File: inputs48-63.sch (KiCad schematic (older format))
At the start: 160 parts

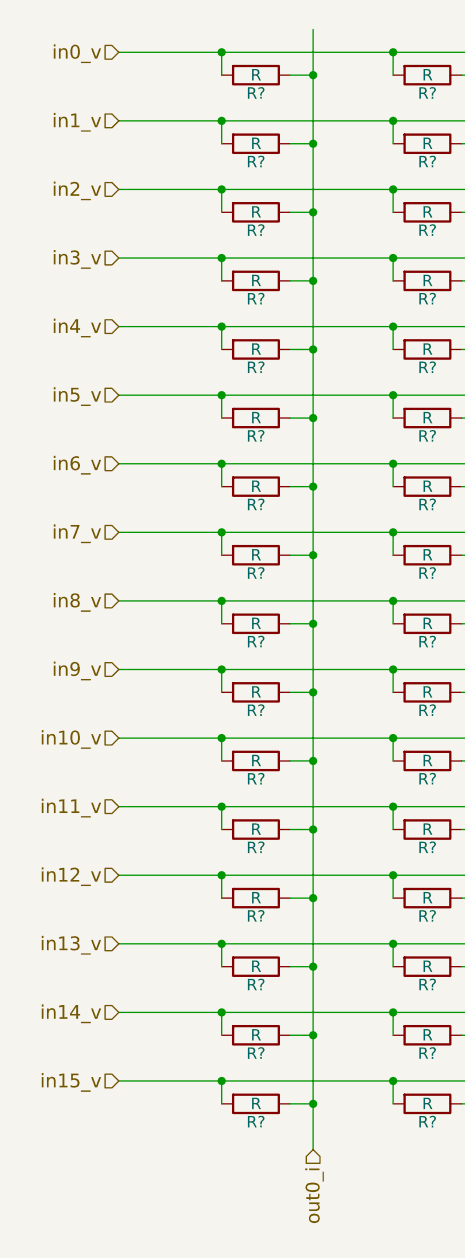
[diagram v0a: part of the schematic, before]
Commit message: updated labels for schematics 32-47 and 48-63
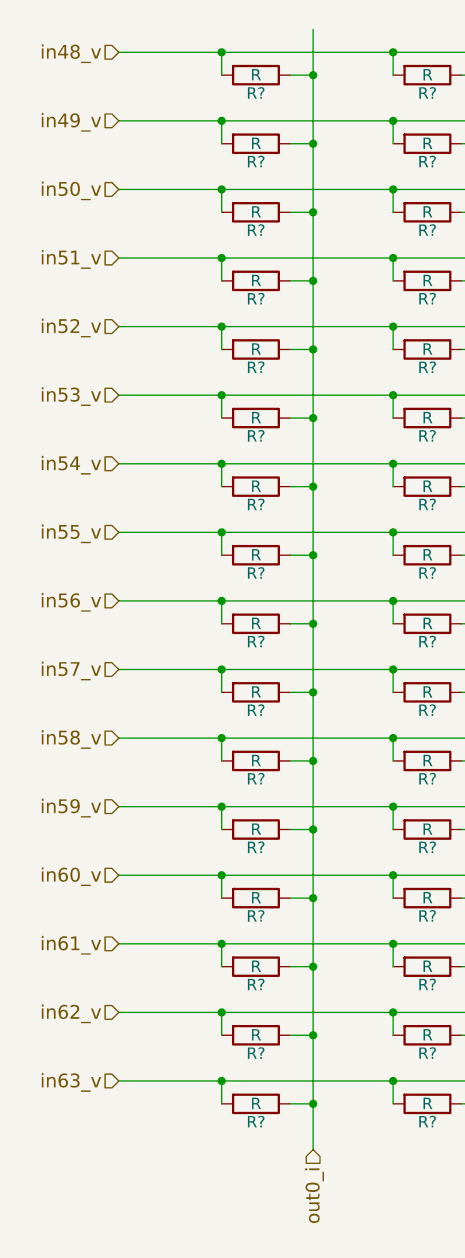
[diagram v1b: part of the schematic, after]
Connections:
- net labels added: in48_v, in49_v, in50_v, in51_v, in52_v, in53_v, in54_v, in55_v, in56_v, in57_v, in58_v, in59_v, in60_v, in61_v, in62_v, in63_v
- net labels removed: in0_v, in10_v, in11_v, in12_v, in13_v, in14_v, in15_v, in1_v, in2_v, in3_v, in4_v, in5_v, in6_v, in7_v, in8_v, in9_v
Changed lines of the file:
@@
 $EndDescr
 Text HLabel 1900 1050 0    60   Input ~ 0
-in0_v
+in48_v
 Text HLabel 1900 1350 0    60   Input ~ 0
-in1_v
+in49_v
 Text HLabel 1900 1650 0    60   Input ~ 0
-in2_v
+in50_v
 Text HLabel 1900 1950 0    60   Input ~ 0
-in3_v
+in51_v
 Text HLabel 1900 2250 0    60   Input ~ 0
-in4_v
+in52_v
 Text HLabel 1900 2550 0    60   Input ~ 0
-in5_v
+in53_v
 Text HLabel 1900 2850 0    60   Input ~ 0
-in6_v
+in54_v
 Text HLabel 1900 3150 0    60   Input ~ 0
-in7_v
+in55_v
 Text HLabel 1900 3450 0    60   Input ~ 0
-in8_v
+in56_v
 Text HLabel 1900 3750 0    60   Input ~ 0
-in9_v
+in57_v
 Text HLabel 1900 4050 0    60   Input ~ 0
-in10_v
+in58_v
 Text HLabel 1900 4350 0    60   Input ~ 0
-in11_v
+in59_v
 Text HLabel 1900 4650 0    60   Input ~ 0
-in12_v
+in60_v
 Text HLabel 1900 4950 0    60   Input ~ 0
-in13_v
+in61_v
 Text HLabel 1900 5250 0    60   Input ~ 0
-in14_v
+in62_v
 Text HLabel 1900 5550 0    60   Input ~ 0
-in15_v
+in63_v
 Text HLabel 2750 5850 3    60   Input ~ 0
 out0_i

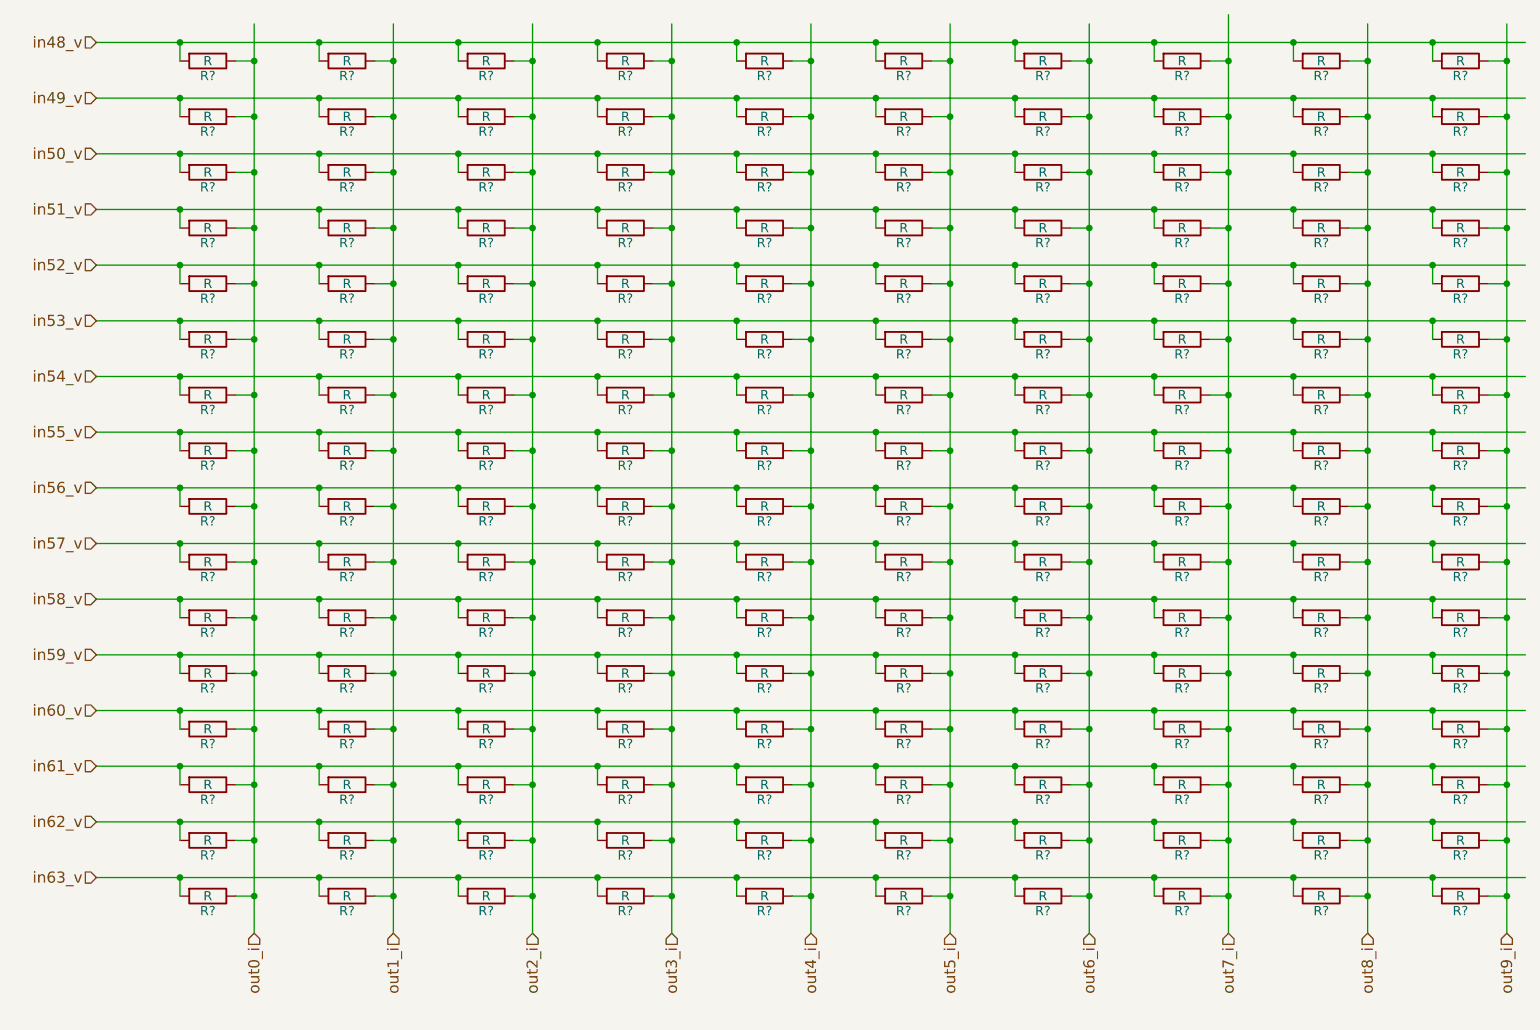
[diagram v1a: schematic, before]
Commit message: Updated resistors 32-63
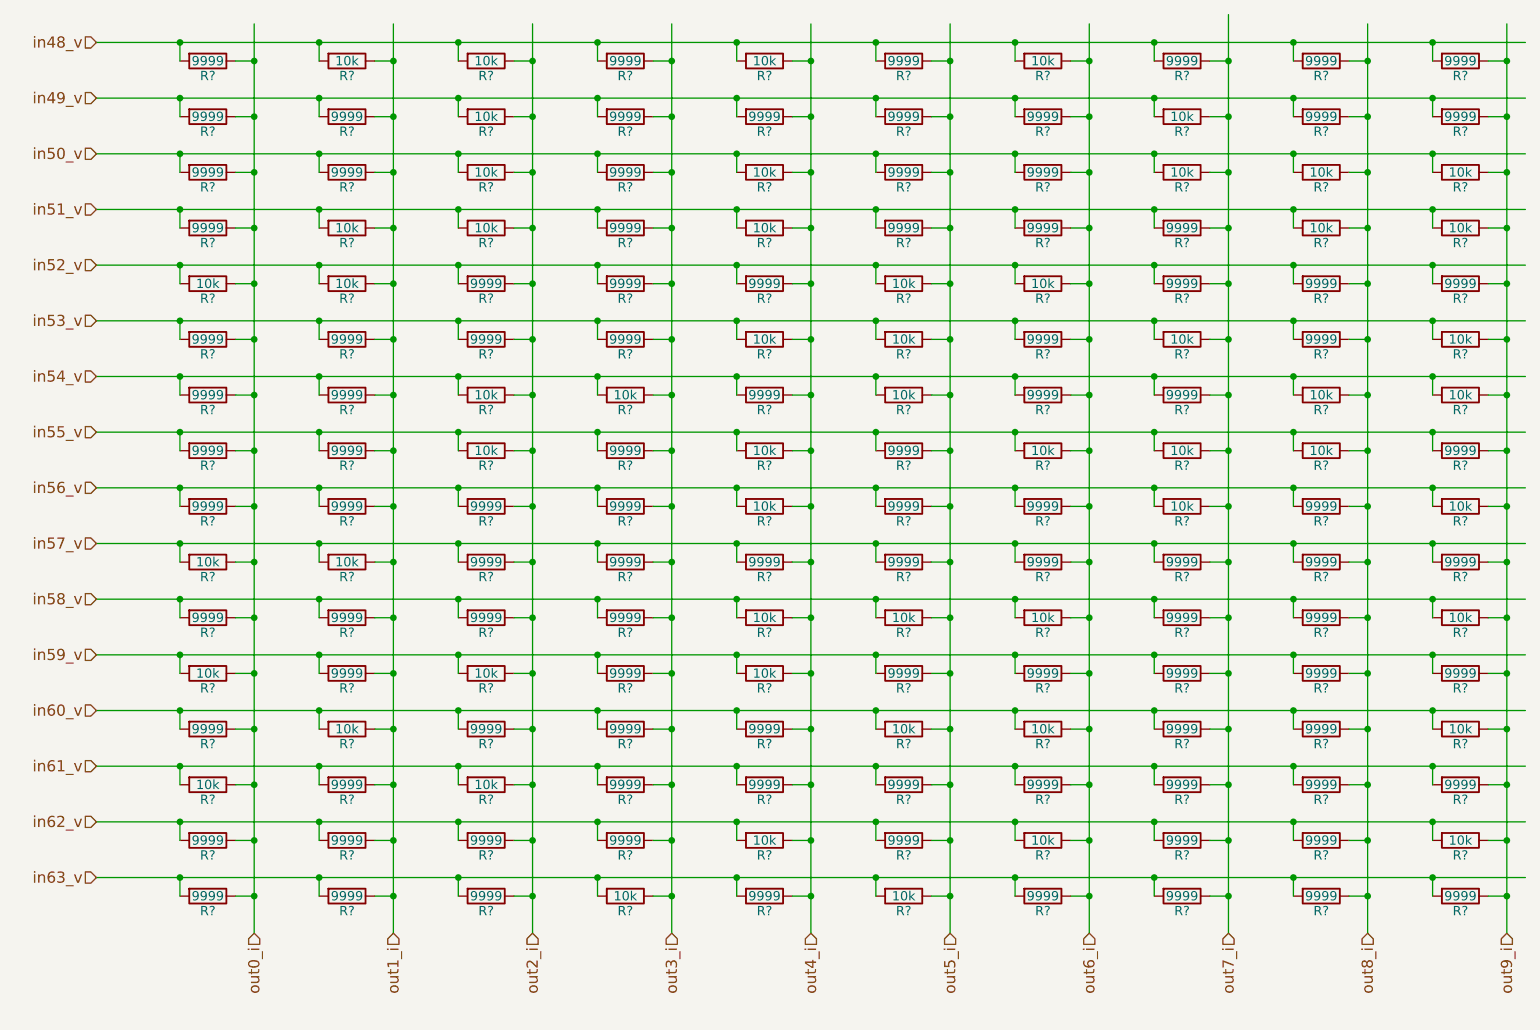
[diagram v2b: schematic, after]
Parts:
- R? (x103): value R -> 9999
- R? (x57): value R -> 10k

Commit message: Finished R48-R63
Now to do the connector and provide power to the op amps
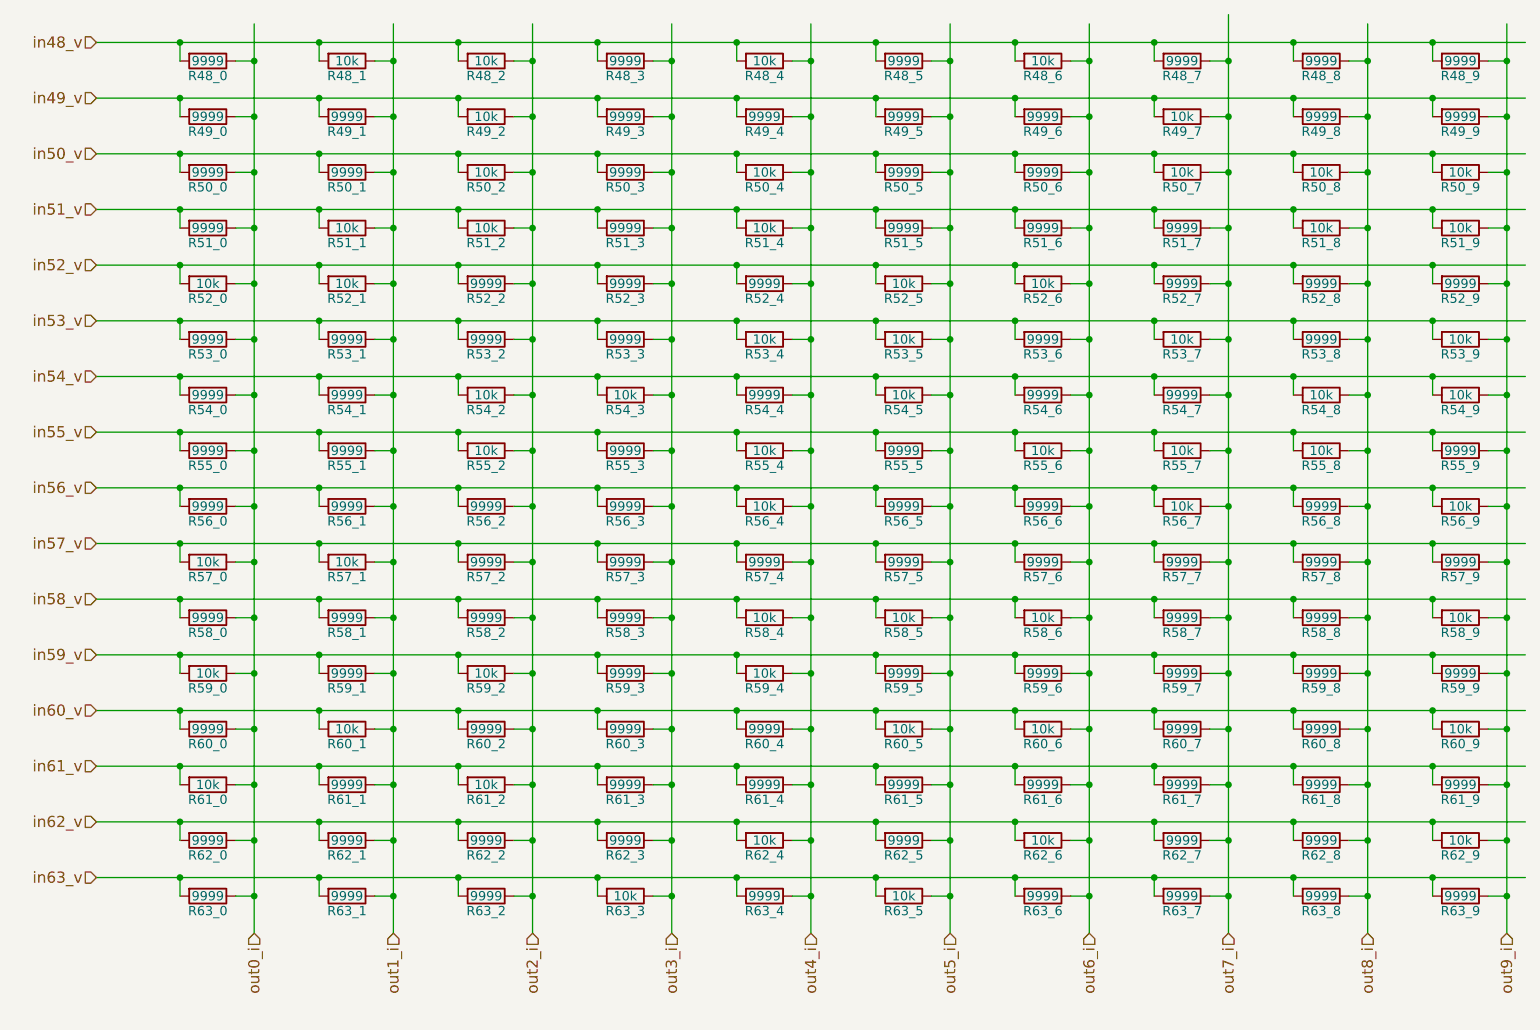
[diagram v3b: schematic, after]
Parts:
- gave numbers to parts that had none: 160

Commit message: Added footprints, finished schematic, began PCB layout
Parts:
- R48_0, R48_1, R48_2, R48_3, R48_4, R48_5, R48_6, R48_7, R48_8, R48_9, R49_0, R49_1, R49_2, R49_3, R49_4, R49_5, R49_6, R49_7, R49_8, R49_9, R50_0, R50_1, R50_2, R50_3, R50_4, R50_5, R50_6, R50_7, R50_8, R50_9, R51_0, R51_1, R51_2, R51_3, R51_4, R51_5, R51_6, R51_7, R51_8, R51_9, R52_0, R52_1, R52_2, R52_3, R52_4, R52_5, R52_6, R52_7, R52_8, R52_9, R53_0, R53_1, R53_2, R53_3, R53_4, R53_5, R53_6, R53_7, R53_8, R53_9, R54_0, R54_1, R54_2, R54_3, R54_4, R54_5, R54_6, R54_7, R54_8, R54_9, R55_0, R55_1, R55_2, R55_3, R55_4, R55_5, R55_6, R55_7, R55_8, R55_9, R56_0, R56_1, R56_2, R56_3, R56_4, R56_5, R56_6, R56_7, R56_8, R56_9, R57_0, R57_1, R57_2, R57_3, R57_4, R57_5, R57_6, R57_7, R57_8, R57_9, R58_0, R58_1, R58_2, R58_3, R58_4, R58_5, R58_6, R58_7, R58_8, R58_9, R59_0, R59_1, R59_2, R59_3, R59_4, R59_5, R59_6, R59_7, R59_8, R59_9, R60_0, R60_1, R60_2, R60_3, R60_4, R60_5, R60_6, R60_7, R60_8, R60_9, R61_0, R61_1, R61_2, R61_3, R61_4, R61_5, R61_6, R61_7, R61_8, R61_9, R62_0, R62_1, R62_2, R62_3, R62_4, R62_5, R62_6, R62_7, R62_8, R62_9, R63_0, R63_1, R63_2, R63_3, R63_4, R63_5, R63_6, R63_7, R63_8, R63_9: footprint (none) -> Resistors_SMD:R_1206

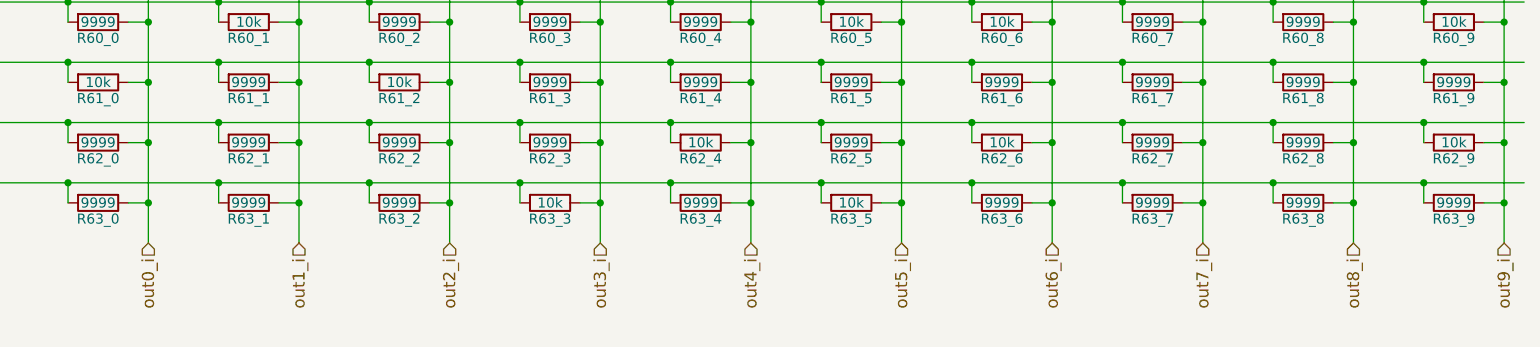
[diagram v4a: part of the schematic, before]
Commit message: fixed resistor schematic errors
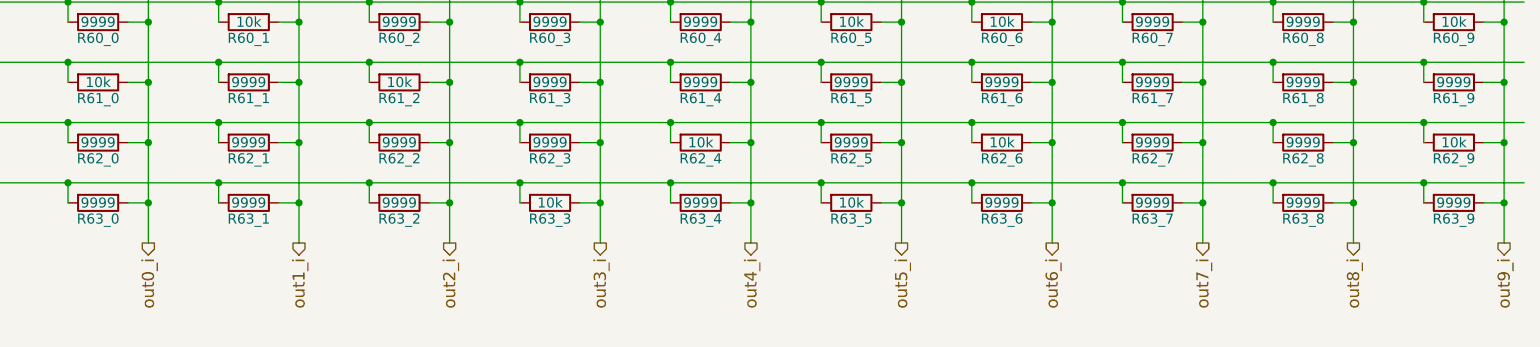
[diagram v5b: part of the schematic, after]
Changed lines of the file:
@@
 Text HLabel 1900 5550 0    60   Input ~ 0
 in63_v
-Text HLabel 2750 5850 3    60   Input ~ 0
+Text HLabel 2750 5850 3    60   Output ~ 0
 out0_i
-Text HLabel 3500 5850 3    60   Input ~ 0
+Text HLabel 3500 5850 3    60   Output ~ 0
 out1_i
-Text HLabel 4250 5850 3    60   Input ~ 0
+Text HLabel 4250 5850 3    60   Output ~ 0
 out2_i
-Text HLabel 5000 5850 3    60   Input ~ 0
+Text HLabel 5000 5850 3    60   Output ~ 0
 out3_i
-Text HLabel 5750 5850 3    60   Input ~ 0
+Text HLabel 5750 5850 3    60   Output ~ 0
 out4_i
-Text HLabel 6500 5850 3    60   Input ~ 0
+Text HLabel 6500 5850 3    60   Output ~ 0
 out5_i
-Text HLabel 7250 5850 3    60   Input ~ 0
+Text HLabel 7250 5850 3    60   Output ~ 0
 out6_i
-Text HLabel 8000 5850 3    60   Input ~ 0
+Text HLabel 8000 5850 3    60   Output ~ 0
 out7_i
-Text HLabel 8750 5850 3    60   Input ~ 0
+Text HLabel 8750 5850 3    60   Output ~ 0
 out8_i
-Text HLabel 9500 5850 3    60   Input ~ 0
+Text HLabel 9500 5850 3    60   Output ~ 0
 out9_i
 $Comp
